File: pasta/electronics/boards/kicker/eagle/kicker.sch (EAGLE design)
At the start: 89 parts, among them Q101 FJT44TF, Q102 TPH3300CNH, Q201 IXYT55N120A4HV, Q202 IXYT55N120A4HV, T101 WE_FB_EFD25-750310988, U101 LT3748IMS, U201 UCC27532, U202 UCC27532, U203 NCP785AH150T1G, U204 NCP785AH150T1G, U301 AMC1304L05DWDW0016B_HV, Y301 DSC1123CI2-020.0000

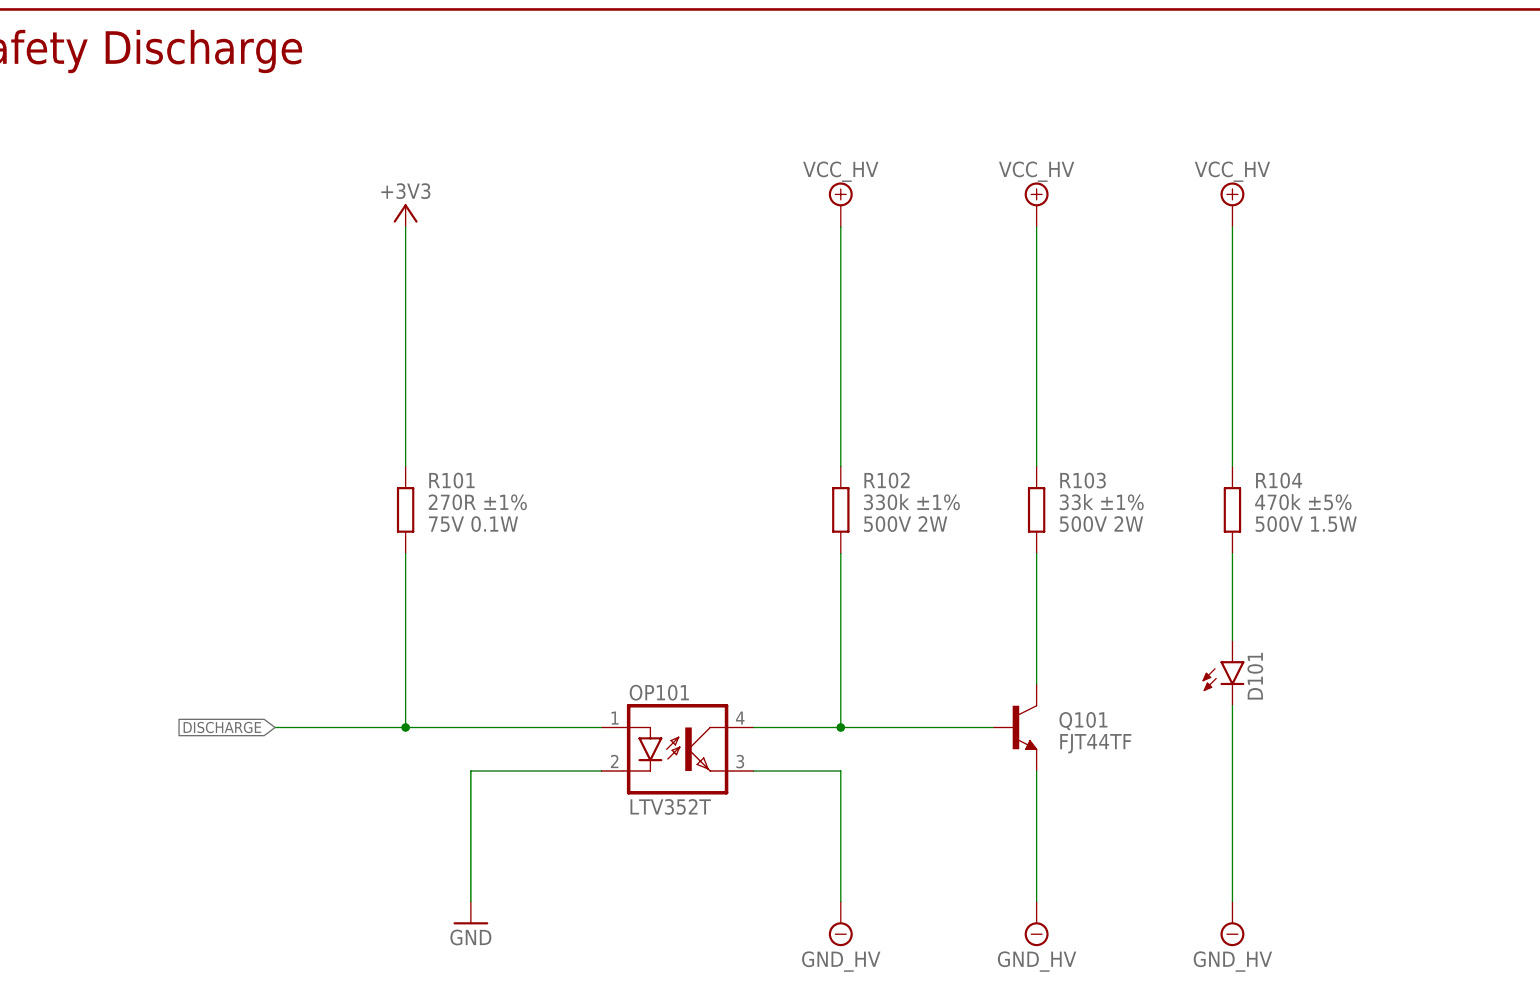
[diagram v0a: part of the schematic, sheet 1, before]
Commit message: pasta: kicker: fix some bugs in schematics
- U203 had the wrong MPN (now replaced by a 3V3 LDO)
- Increased input capacitor of U203 to 10u 50V (previously 330n 250V)
- Changed title of U203 block in schematics to be more fitting
- Fixed MPN of optocouplers (value was right, but MPN was wrong)
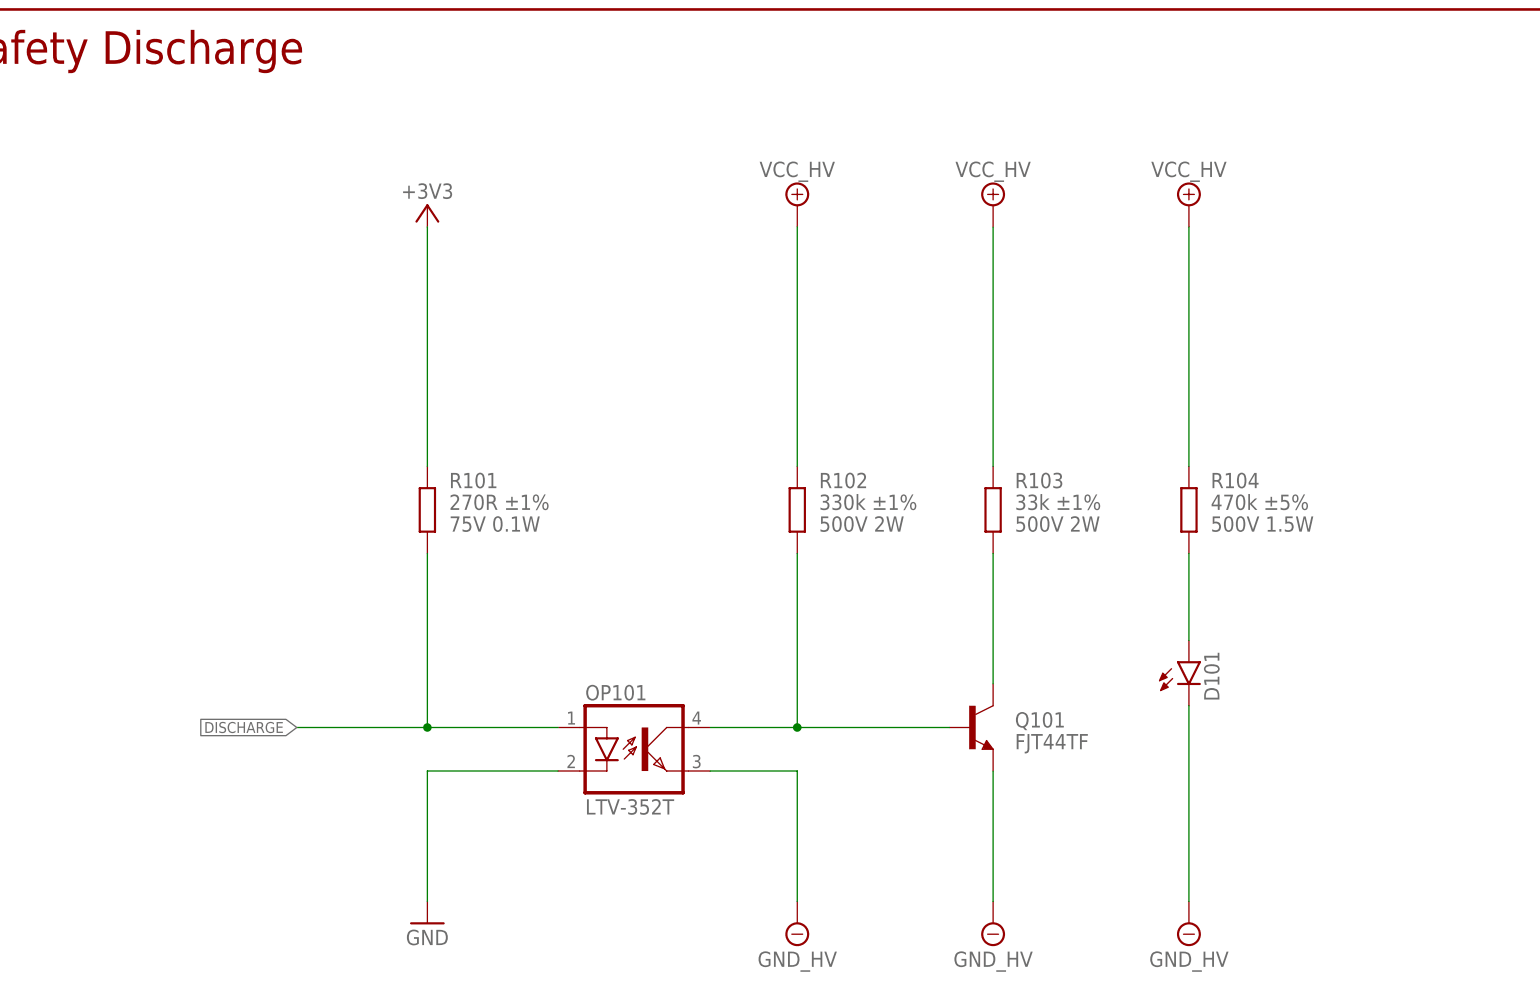
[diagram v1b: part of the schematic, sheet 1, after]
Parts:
- C205: value C(1210) -> 10u ±20% 50V X5R; device capacitors:C(1210) -> capacitors:C(10UF,50V,1206); CAPACITANCE 330n -> (none); DIELECTRIC X7T -> (none); LINE1 330n ±10% -> (none); LINE2 X7T 250V -> (none); MF TDK -> (none); MPN C3225X7T2E334K200AA -> (none); TOLERANCE ±10% -> (none); VOLTAGE 250V -> (none)
- OP101, OP201, OP202: value LTV352T -> LTV-352T; device kicker:LTV816S -> kicker:LTV-352T
- U203: value NCP785AH150T1G -> NCP785AH33T1G; device kicker:NCP785AH150T1G -> kicker:NCP785AH33T1G
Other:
- note added: "Low Side 3V3 Generation"
- note removed: "ADC Supply Voltage (Low Side)"
- note removed: "EN has internal pull-up"
- moved on the sheet: D101, OP101, Q101, R101, R102, R103, R104
